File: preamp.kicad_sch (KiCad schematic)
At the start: 19 parts, among them U3 TL972QDRQ1

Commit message: Resnap text to grid + add .gitignore
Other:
- company: (none) -> Tachyon PCBAs
- title: (none) -> Microphone Preamplifier
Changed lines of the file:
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@@
 	(paper "A4")
 	(title_block
-		(date "2024-09-12")
+		(title "Microphone Preamplifier")
+		(date "2024-09-15")
+		(rev "1")
+		(company "Tachyon PCBAs")
+		(comment 1 "first try surely")
 	)
 	(junction
@@
 	(text "RIGHT"
 		(exclude_from_sim no)
-		(at 80.264 124.714 0)
+		(at 80.01 124.46 0)
 		(effects
 			(font
@@
 	(text "LEFT"
 		(exclude_from_sim no)
-		(at 79.756 78.74 0)
+		(at 80.01 78.74 0)
 		(effects
 			(font
@@
 	(text "Mic Preamp"
 		(exclude_from_sim no)
-		(at 140.208 36.83 0)
+		(at 140.335 36.83 0)
 		(effects
 			(font
@@
 	(text "C20\ndischarge\npath"
 		(exclude_from_sim no)
-		(at 141.732 129.794 0)
+		(at 141.605 129.54 0)
 		(effects
 			(font
@@
 	(text "Calculations for this preamp circuit follow TI's white paper for electret microphone preamps at https://www.ti.com/lit/ug/tidu765/tidu765.pdf\nSimulations can also be found in ./sim/Preamp2.*"
 		(exclude_from_sim no)
-		(at 70.866 152.146 0)
+		(at 71.12 152.4 0)
 		(effects
 			(font
@@
 	(text "Voltage Rails"
 		(exclude_from_sim no)
-		(at 167.894 75.692 0)
+		(at 168.275 75.565 0)
 		(effects
 			(font
@@
 	(text "Preamp"
 		(exclude_from_sim no)
-		(at 73.914 49.276 0)
+		(at 74.295 48.895 0)
 		(effects
 			(font
@@
 	(text "C16\ndischarge\npath"
 		(exclude_from_sim no)
-		(at 141.478 84.582 0)
-		(effects
-			(font
+		(at 141.605 84.455 0)
+		(effects
+			(font

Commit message: Started defining components
Man going down the capacitor dielectric rabbit hole eats up SO MUCH TIME
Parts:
- added C17: 4.7u, Capacitor_SMD:C_1206_3216Metric_Pad1.33x1.80mm_HandSolder, symbol Device:C
- added D4: PESD3V3Y1BSF, Diode_SMD:Nexperia_DSN0603-2_0.6x0.3mm_P0.4mm, symbol Device:D_TVS
- added R17, R20: 100k, Resistor_SMD:R_0603_1608Metric_Pad0.98x0.95mm_HandSolder, symbol Device:R
- C14, C18: Mouser Part Number (none) -> 77-VJ0603D680FXPAJ
- C15, C16, C19, C20: footprint Capacitor_SMD:C_0603_1608Metric_Pad1.08x0.95mm_HandSolder -> Capacitor_SMD:C_1206_3216Metric_Pad1.33x1.80mm_HandSolder; Mouser Part Number (none) -> 581-TAJA475K016R
- C22: footprint Capacitor_SMD:C_0603_1608Metric_Pad1.08x0.95mm_HandSolder -> Capacitor_SMD:C_0805_2012Metric_Pad1.18x1.45mm_HandSolder; Mouser Part Number (none) -> 74-TMCP1E104KTRF
- C23: footprint Capacitor_SMD:C_0603_1608Metric_Pad1.08x0.95mm_HandSolder -> Capacitor_SMD:C_1206_3216Metric_Pad1.33x1.80mm_HandSolder; Mouser Part Number (none) -> 581-TAJA105K020TNJ
- R14, R15, R16, R18, R19, R21, R22, R23, R25, R26: footprint (none) -> Resistor_SMD:R_0603_1608Metric_Pad0.98x0.95mm_HandSolder
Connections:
- net VCC: now also D4.2 (A2), R20.1
- net VCOM: now also C17.2, R17.1, R20.2; no longer C22.2, C23.2, R19.2, R26.2, U3.4 (V-)
- new net GND: C17.1, C22.2, C23.2, D4.1 (A1), R17.2, R19.2, R26.2, U3.4 (V-)
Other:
- note added: "Additional ESD protection to avoid microphonic effects"
- note added: "Backup VCOM reference"

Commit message: Fully define components
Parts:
- R14, R21: Mouser Part Number (none) -> 652-CR0603FX-1004ELF
- R15, R22: Mouser Part Number (none) -> 667-ERA-3AEB5901V
- R16, R23: Mouser Part Number (none) -> 667-ERA-3AEB183V
- R17, R19, R20, R26: Mouser Part Number (none) -> 603-RT0603FRE10100KL
- R18, R25: Mouser Part Number (none) -> 791-RMC1/16K49R9FTP
- U3: Mouser Part Number (none) -> 595-TL972QDRQ1
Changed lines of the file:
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@@
 			)
 		)
-		(property "Datasheet" "~"
+		(property "Datasheet" "https://www.mouser.com/datasheet/2/210/Kamaya_RMC_series_8_2022-3032447.pdf"
 			(at 125.73 123.19 0)
 			(effects
@@
 		)
 		(property "Description" "Resistor"
+			(at 125.73 123.19 0)
+			(effects
+				(font
+					(size 1.27 1.27)
+				)
+				(hide yes)
+			)
+		)
+		(property "Mouser Part Number" "791-RMC1/16K49R9FTP"
 			(at 125.73 123.19 0)
 			(effects
@@
 			)
 		)
-		(property "Datasheet" "~"
+		(property "Datasheet" "https://www.mouser.com/datasheet/2/447/PYu_RT_1_to_0_01_RoHS_L_15-3461507.pdf"
 			(at 149.86 83.82 0)
 			(effects
@@
 		)
 		(property "Description" "Resistor"
+			(at 149.86 83.82 0)
+			(effects
+				(font
+					(size 1.27 1.27)
+				)
+				(hide yes)
+			)
+		)
+		(property "Mouser Part Number" "603-RT0603FRE10100KL"
 			(at 149.86 83.82 0)
 			(effects
@@
 			)
 		)
-		(property "Datasheet" "~"
+		(property "Datasheet" "https://www.mouser.com/datasheet/2/315/AOA0000C307-1149632.pdf"
 			(at 111.76 69.85 0)
 			(effects
@@
 		)
 		(property "Description" "Resistor"
+			(at 111.76 69.85 0)
+			(effects
+				(font
+					(size 1.27 1.27)
+				)
+				(hide yes)
+			)
+		)
+		(property "Mouser Part Number" "667-ERA-3AEB183V"
 			(at 111.76 69.85 0)
 			(effects
@@
 			)
 		)
+		(property "Mouser Part Number" "595-TL972QDRQ1 "
+			(at 179.07 95.25 0)
+			(effects
+				(font
+					(size 1.27 1.27)
+				)
+				(hide yes)
+			)
+		)
 		(pin "5"
 		)
@@
 			)
 		)
-		(property "Datasheet" "~"
+		(property "Datasheet" "https://www.mouser.com/datasheet/2/54/cr-1858361.pdf"
 			(at 111.76 113.03 0)
 			(effects
@@
 			)
 		)
+		(property "Mouser Part Number" "652-CR0603FX-1004ELF"
+			(at 111.76 113.03 0)
+			(effects
+				(font
+					(size 1.27 1.27)
+				)
+				(hide yes)
+			)
+		)
 		(pin "2"
 		)
@@
 			)
 		)
-		(property "Datasheet" "~"
+		(property "Datasheet" "https://www.mouser.com/datasheet/2/315/AOA0000C307-1149632.pdf"
 			(at 111.76 115.57 0)
 			(effects
@@
 		)
 		(property "Description" "Resistor"
+			(at 111.76 115.57 0)
+			(effects
+				(font
+					(size 1.27 1.27)
+				)
+				(hide yes)
+			)
+		)
+		(property "Mouser Part Number" "667-ERA-3AEB183V"
 			(at 111.76 115.57 0)
 			(effects
@@
 			)
 		)
+		(property "Mouser Part Number" "595-TL972QDRQ1 "
+			(at 111.76 123.19 0)
+			(effects
+				(font
+					(size 1.27 1.27)
+				)
+				(hide yes)
+			)
+		)
 		(pin "5"
 		)
@@
 			)
 		)
+		(property "Mouser Part Number" "595-TL972QDRQ1 "
+			(at 111.76 77.47 0)
+			(effects
+				(font
+					(size 1.27 1.27)
+				)
+				(hide yes)
+			)
+		)
 		(pin "5"
 		)
@@
 			)
 		)
-		(property "Datasheet" "~"
+		(property "Datasheet" "https://www.mouser.com/datasheet/2/447/PYu_RT_1_to_0_01_RoHS_L_15-3461507.pdf"
 			(at 228.6 90.17 0)
 			(effects
@@
 		)
 		(property "Description" "Resistor"
+			(at 228.6 90.17 0)
+			(effects
+				(font
+					(size 1.27 1.27)
+				)
+				(hide yes)
+			)
+		)
+		(property "Mouser Part Number" "603-RT0603FRE10100KL"
 			(at 228.6 90.17 0)
 			(effects
@@
 			)
 		)
-		(property "Datasheet" "~"
+		(property "Datasheet" "https://www.mouser.com/datasheet/2/315/AOA0000C307-1149632.pdf"
 			(at 92.71 68.58 0)
 			(effects
@@
 		)
 		(property "Description" "Resistor"
+			(at 92.71 68.58 0)
+			(effects
+				(font
+					(size 1.27 1.27)
+				)
+				(hide yes)
+			)
+		)
+		(property "Mouser Part Number" "667-ERA-3AEB5901V"
 			(at 92.71 68.58 0)
 			(effects
@@
 			)
 		)
-		(property "Datasheet" "~"
+		(property "Datasheet" "https://www.mouser.com/datasheet/2/210/Kamaya_RMC_series_8_2022-3032447.pdf"
 			(at 125.73 77.47 0)
 			(effects
@@
 		)
 		(property "Description" "Resistor"
+			(at 125.73 77.47 0)
+			(effects
+				(font
+					(size 1.27 1.27)
+				)
+				(hide yes)
+			)
+		)
+		(property "Mouser Part Number" "791-RMC1/16K49R9FTP"
 			(at 125.73 77.47 0)
 			(effects
@@
 			)
 		)
-		(property "Datasheet" "~"
+		(property "Datasheet" "https://www.mouser.com/datasheet/2/315/AOA0000C307-1149632.pdf"
 			(at 92.71 114.3 0)
 			(effects
@@
 		)
 		(property "Description" "Resistor"
+			(at 92.71 114.3 0)
+			(effects
+				(font
+					(size 1.27 1.27)
+				)
+				(hide yes)
+			)
+		)
+		(property "Mouser Part Number" "667-ERA-3AEB5901V"
 			(at 92.71 114.3 0)
 			(effects
@@
 			)
 		)
-		(property "Datasheet" "~"
+		(property "Datasheet" "https://www.mouser.com/datasheet/2/447/PYu_RT_1_to_0_01_RoHS_L_15-3461507.pdf"
 			(at 149.86 129.54 0)
 			(effects
@@
 		)
 		(property "Description" "Resistor"
+			(at 149.86 129.54 0)
+			(effects
+				(font
+					(size 1.27 1.27)
+				)
+				(hide yes)
+			)
+		)
+		(property "Mouser Part Number" "603-RT0603FRE10100KL"
 			(at 149.86 129.54 0)
 			(effects
@@
 			)
 		)
-		(property "Datasheet" "~"
+		(property "Datasheet" "https://www.mouser.com/datasheet/2/447/PYu_RT_1_to_0_01_RoHS_L_15-3461507.pdf"
 			(at 228.6 100.33 0)
 			(effects
@@
 			)
 		)
+		(property "Mouser Part Number" "603-RT0603FRE10100KL"
+			(at 228.6 100.33 0)
+			(effects
+				(font
+					(size 1.27 1.27)
+				)
+				(hide yes)
+			)
+		)
 		(pin "2"
 		)
@@
 			)
 		)
-		(property "Datasheet" "~"
+		(property "Datasheet" "https://www.mouser.com/datasheet/2/54/cr-1858361.pdf"
 			(at 111.76 67.31 0)
 			(effects
@@
 			(at 111.76 67.31 0)
 			(effects
+				(font
+					(size 1.27 1.27)
+				)
+				(hide yes)
+			)
+		)
+		(property "Mouser Part Number" "652-CR0603FX-1004ELF"
+			(at 111.76 67.31 0)
+			(effects

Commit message: Add analog volume control
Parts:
- removed R16, R23: 18k, Resistor_SMD:R_0603_1608Metric_Pad0.98x0.95mm_HandSolder, symbol Device:R
- added VR1: P140KH1-Y20AR20K, binauralmic:P140KH1Y20AR20K, symbol binauralmic:P140KH1-Y20AR20K
- D4: Mouser Part Number (none) -> 771-PESD3V3Y1BSFYL
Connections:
- net VN_{L}: now also VR1.R11 (CCW_1), VR1.R12 (WIPER_1)
- net VN_{R}: now also VR1.R21 (CCW_2), VR1.R22 (WIPER_2)
- net VOUT_{L}: now also VR1.R13 (CW_1)
- net VOUT_{R}: now also VR1.R23 (CW_2)
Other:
- moved on the sheet: C18, C19, C20, R21, R22, R25, R26, U3B

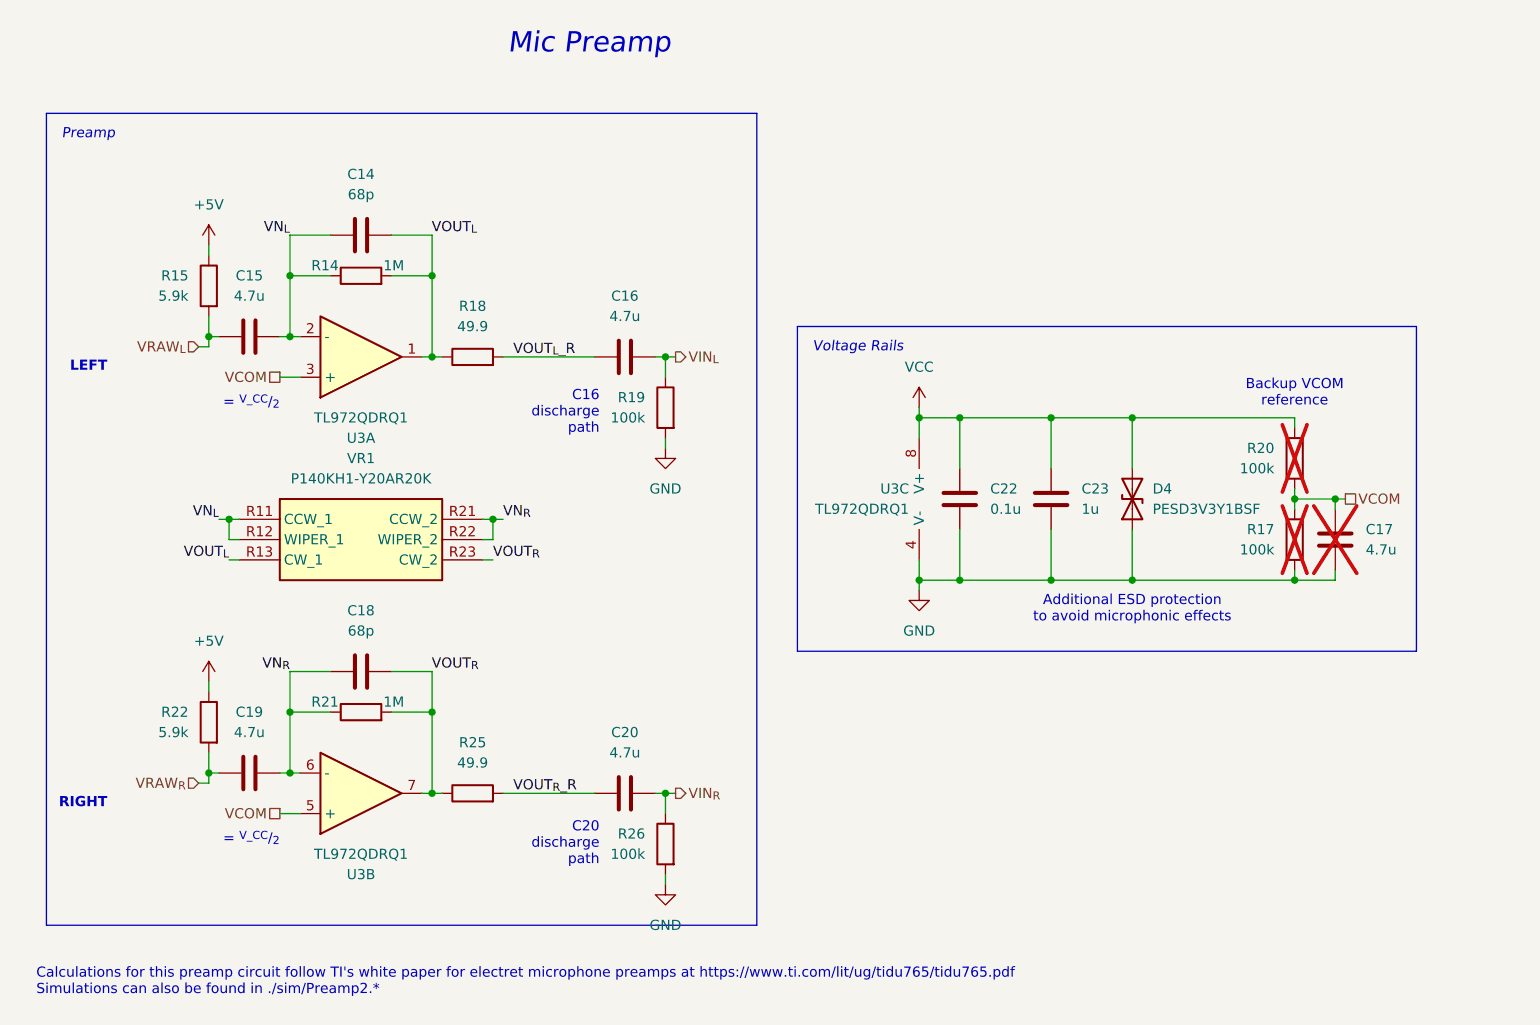
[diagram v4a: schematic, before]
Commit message: Remove potentiometer
Will have to find a different solution for volume control
Just do it OS-side?
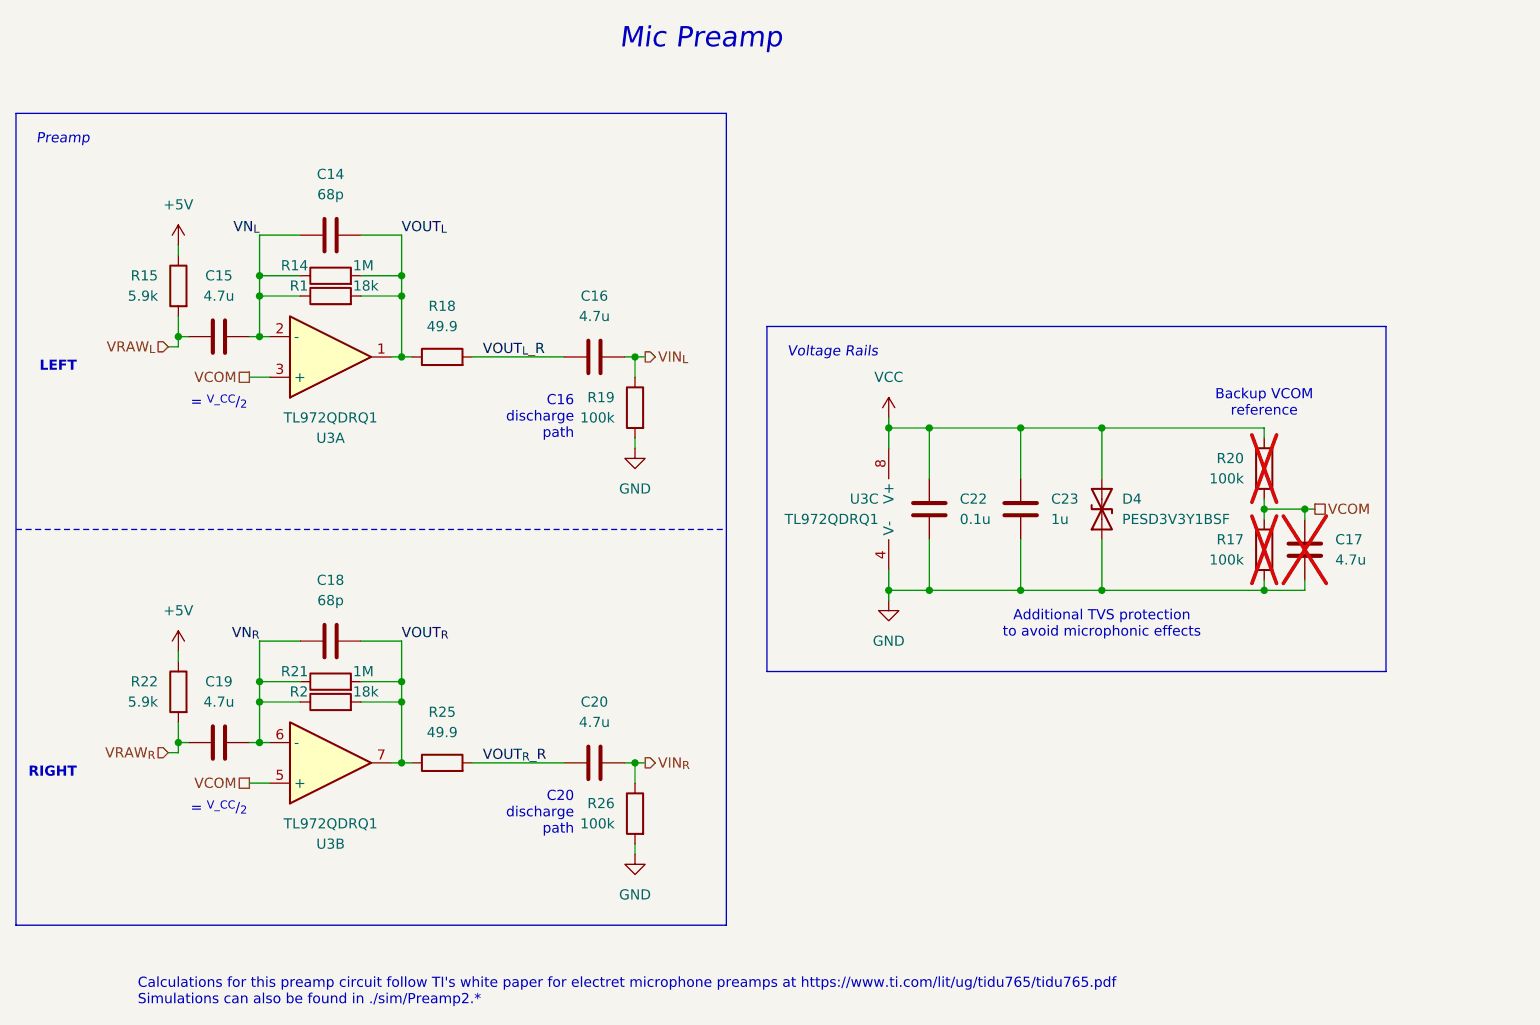
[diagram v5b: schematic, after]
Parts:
- removed VR1: P140KH1-Y20AR20K, binauralmic:P140KH1Y20AR20K, symbol binauralmic:P140KH1-Y20AR20K
- added R1, R2: 18k, Resistor_SMD:R_0603_1608Metric_Pad0.98x0.95mm_HandSolder, symbol Device:R
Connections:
- net VN_{L}: now also R1.1
- net VN_{R}: now also R2.1
- net VOUT_{L}: now also R1.2
- net VOUT_{R}: now also R2.2
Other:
- note added: "Additional TVS protection to avoid microphonic effects"
- note removed: "Additional ESD protection to avoid microphonic effects"
- moved on the sheet: C14, C15, C16, C17, C18, C19, C20, C22, C23, D4, R14, R15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

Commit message: Starting layout
Also why are the mf diodes so small
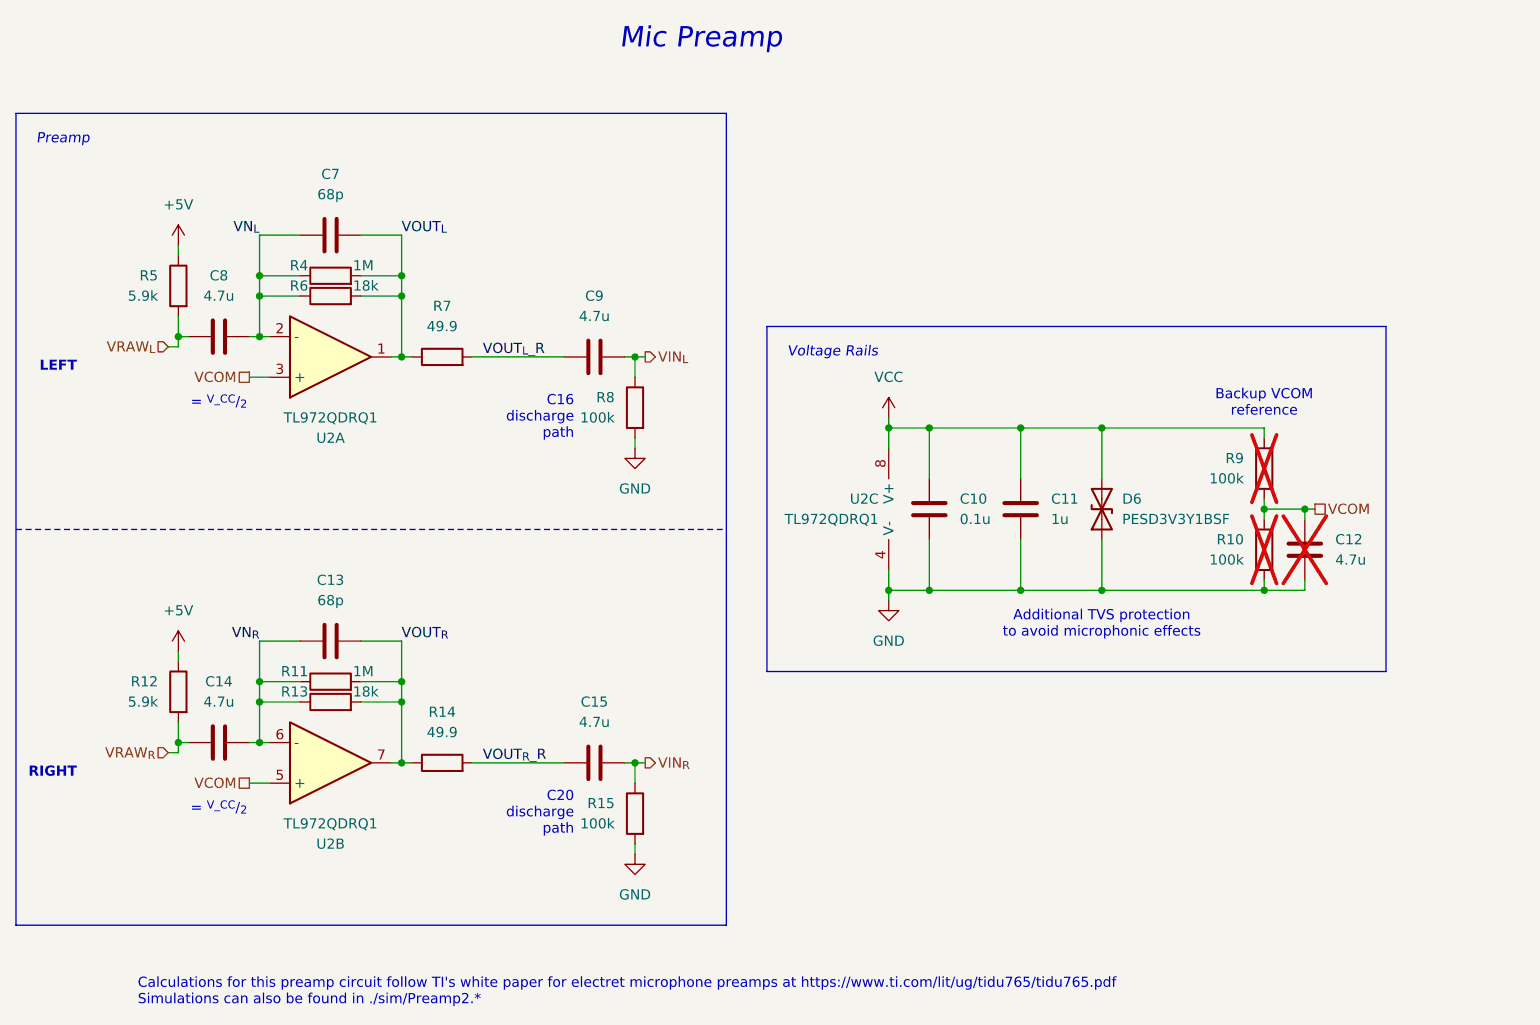
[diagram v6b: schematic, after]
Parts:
- D6: renamed from D4; footprint Diode_SMD:Nexperia_DSN0603-2_0.6x0.3mm_P0.4mm -> Diode_SMD:D_0201_0603Metric_Pad0.64x0.40mm_HandSolder
- renumbered C22 to C10, C23 to C11, C17 to C12, C18 to C13, C19 to C14, C20 to C15, C14 to C7, C15 to C8, C16 to C9, R17 to R10, R21 to R11, R22 to R12, R2 to R13, R25 to R14, R26 to R15, R14 to R4, R15 to R5, R1 to R6, R18 to R7, R19 to R8, R20 to R9, U3 to U2
